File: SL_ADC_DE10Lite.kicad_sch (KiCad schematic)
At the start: 21 parts, among them J1 Conn_02x20_Odd_Even, J2 Conn_02x08_Odd_Even, J3 Conn_02x05_Counter_Clockwise, J5 Conn_02x07_Counter_Clockwise

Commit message: Update net names
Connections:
- net CH_C1: now also IC1.63 (REFCP)
- net DGND: no longer IC1.36 (ASLEEP)
- net REFCP: no longer IC1.63 (REFCP)
- net ASLEEP: now reaches J1.21 (Pin_21)
- net ASLEEP: now also IC1.36 (ASLEEP)
- net GPIO(23)-REFIN/~{WR} renamed GPIO(23)-REFEN/~{WR}
- no-connect marks 7 -> 6
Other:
- moved on the sheet: J2, J3, J5
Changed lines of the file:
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@@
 		(at 44.45 176.53)
 	)
-	(no_connect
-		(at 44.45 156.21)
-	)
 	(wire
 		(pts
@@
 	)
 	(label "CH_A0"
-		(at 102.87 130.81 0)
+		(at 104.14 132.08 0)
 		(effects
 			(font
@@
 	)
 	(label "DGND"
-		(at 102.87 162.56 0)
+		(at 104.14 163.83 0)
 		(effects
 			(font
@@
 	)
 	(label "CH_D0"
-		(at 90.17 146.05 180)
+		(at 91.44 147.32 180)
 		(effects
 			(font
@@
 	)
 	(label "CH_D0"
-		(at 102.87 146.05 0)
+		(at 104.14 147.32 0)
 		(effects
 			(font
@@
 	)
 	(label "DGND"
-		(at 102.87 165.1 0)
+		(at 104.14 166.37 0)
 		(effects
 			(font
@@
 		)
 	)
-	(label "GPIO(23)-REFIN{slash}~{WR}"
+	(label "GPIO(23)-REFEN{slash}~{WR}"
 		(at 57.15 161.29 0)
 		(effects
@@
 		)
 	)
-	(label "GPIO(23)-REFIN{slash}~{WR}"
+	(label "GPIO(23)-REFEN{slash}~{WR}"
 		(at 43.18 67.31 180)
 		(effects
@@
 	)
 	(label "CH_C1"
-		(at 102.87 143.51 0)
+		(at 104.14 144.78 0)
 		(effects
 			(font
@@
 	)
 	(label "CH_A1"
-		(at 90.17 133.35 180)
+		(at 91.44 134.62 180)
 		(effects
 			(font
@@
 	)
 	(label "HVSS"
-		(at 134.62 163.83 0)
+		(at 135.89 165.1 0)
 		(effects
 			(font
@@
 	)
 	(label "AGND"
-		(at 121.92 173.99 180)
+		(at 123.19 175.26 180)
 		(effects
 			(font
@@
 	)
 	(label "AGND"
-		(at 134.62 166.37 0)
+		(at 135.89 167.64 0)
 		(effects
 			(font
@@
 	)
 	(label "HVDD"
-		(at 121.92 158.75 180)
+		(at 123.19 160.02 180)
 		(effects
 			(font
@@
 		)
 	)
+	(label "ASLEEP"
+		(at 44.45 156.21 180)
+		(effects
+			(font
+				(size 1.27 1.27)
+			)
+			(justify right bottom)
+		)
+	)
 	(label "CH_B0"
-		(at 102.87 135.89 0)
+		(at 104.14 137.16 0)
 		(effects
 			(font
@@
 	)
 	(label "DGND"
-		(at 90.17 170.18 180)
+		(at 91.44 171.45 180)
 		(effects
 			(font
@@
 	)
 	(label "DGND"
-		(at 90.17 167.64 180)
+		(at 91.44 168.91 180)
 		(effects
 			(font
@@
 	)
 	(label "CH_C0"
-		(at 90.17 140.97 180)
+		(at 91.44 142.24 180)
 		(effects
 			(font
@@
 	)
 	(label "DGND"
-		(at 102.87 172.72 0)
+		(at 104.14 173.99 0)
 		(effects
 			(font
@@
 	)
 	(label "CH_B1"
-		(at 102.87 138.43 0)
+		(at 104.14 139.7 0)
 		(effects
 			(font
@@
 	)
 	(label "CH_C1"
-		(at 90.17 143.51 180)
+		(at 91.44 144.78 180)
 		(effects
 			(font
@@
 	)
 	(label "DGND"
-		(at 90.17 172.72 180)
+		(at 91.44 173.99 180)
 		(effects
 			(font
@@
 	)
 	(label "DGND"
-		(at 90.17 162.56 180)
+		(at 91.44 163.83 180)
 		(effects
 			(font
@@
 	)
 	(label "DGND"
-		(at 102.87 167.64 0)
+		(at 104.14 168.91 0)
 		(effects
 			(font
@@
 	)
 	(label "AVDD"
-		(at 121.92 161.29 180)
+		(at 123.19 162.56 180)
 		(effects
 			(font
@@
 	)
 	(label "AGND"
-		(at 134.62 171.45 0)
+		(at 135.89 172.72 0)
 		(effects
 			(font
@@
 	)
 	(label "HVDD"
-		(at 134.62 158.75 0)
+		(at 135.89 160.02 0)
 		(effects
 			(font
@@
 	)
 	(label "HVSS"
-		(at 121.92 163.83 180)
+		(at 123.19 165.1 180)
 		(effects
 			(font
@@
 	)
 	(label "CH_A0"
-		(at 90.17 130.81 180)
+		(at 91.44 132.08 180)
 		(effects
 			(font
@@
 	)
 	(label "CH_B0"
-		(at 90.17 135.89 180)
+		(at 91.44 137.16 180)
 		(effects
 			(font
@@
 	)
 	(label "DGND"
-		(at 90.17 165.1 180)
+		(at 91.44 166.37 180)
 		(effects
 			(font
@@
 	)
 	(label "CH_D1"
-		(at 102.87 148.59 0)
+		(at 104.14 149.86 0)
 		(effects
 			(font
@@
 	)
 	(label "AGND"
-		(at 121.92 168.91 180)
+		(at 123.19 170.18 180)
 		(effects
 			(font
@@
 		)
 	)
-	(label "DGND"
+	(label "ASLEEP"
 		(at 116.84 72.39 0)
 		(effects
@@
 	)
 	(label "CH_C0"
-		(at 102.87 140.97 0)
+		(at 104.14 142.24 0)
 		(effects
 			(font
@@
 	)
 	(label "CH_B1"
-		(at 90.17 138.43 180)
+		(at 91.44 139.7 180)
 		(effects
 			(font
@@
 	)
 	(label "CH_A1"
-		(at 102.87 133.35 0)
+		(at 104.14 134.62 0)
 		(effects
 			(font
@@
 	)
 	(label "AGND"
-		(at 134.62 173.99 0)
+		(at 135.89 175.26 0)
 		(effects
 			(font
@@
 	)
 	(label "AGND"
-		(at 121.92 171.45 180)
+		(at 123.19 172.72 180)
 		(effects
 			(font
@@
 	)
 	(label "AGND"
-		(at 121.92 166.37 180)
+		(at 123.19 167.64 180)
 		(effects
 			(font
@@
 		)
 	)
-	(label "REFCP"
+	(label "CH_C1"
 		(at 63.5 36.83 90)
 		(effects
@@
 	)
 	(label "AVDD"
-		(at 134.62 161.29 0)
+		(at 135.89 162.56 0)
 		(effects
 			(font
@@
 	)
 	(label "CH_D1"
-		(at 90.17 148.59 180)
+		(at 91.44 149.86 180)
 		(effects
 			(font
@@
 	)
 	(label "AGND"
-		(at 134.62 168.91 0)
+		(at 135.89 170.18 0)
 		(effects
 			(font
@@
 	)
 	(label "DGND"
-		(at 102.87 170.18 0)
+		(at 104.14 171.45 0)
 		(effects
 			(font
@@
 	(symbol
 		(lib_id "Connector_Generic:Conn_02x05_Counter_Clockwise")
-		(at 95.25 167.64 0)
+		(at 96.52 168.91 0)
 		(unit 1)
 		(body_style 1)
@@
 		(fields_autoplaced yes)
 		(property "Reference" "J3"
-			(at 96.52 156.21 0)
+			(at 97.79 157.48 0)
 			(show_name no)
 			(do_not_autoplace no)
@@
 		)
 		(property "Value" "Conn_02x05_Counter_Clockwise"
-			(at 96.52 158.75 0)
+			(at 97.79 160.02 0)
 			(show_name no)
 			(do_not_autoplace no)
@@
 		)
 		(property "Footprint" "Connector_PinHeader_2.54mm:PinHeader_2x05_P2.54mm_Vertical"
-			(at 95.25 167.64 0)
+			(at 96.52 168.91 0)
 			(hide yes)
 			(show_name no)
@@
 		)
 		(property "Datasheet" ""
-			(at 95.25 167.64 0)
+			(at 96.52 168.91 0)
 			(hide yes)
 			(show_name no)
@@
 		)
 		(property "Description" "Generic connector, double row, 02x05, counter clockwise pin numbering scheme (similar to DIP package numbering), script generated (kicad-library-utils/schlib/autogen/connector/)"
-			(at 95.25 167.64 0)
+			(at 96.52 168.91 0)
 			(hide yes)
 			(show_name no)
@@
 	(symbol
 		(lib_id "Connector_Generic:Conn_02x07_Counter_Clockwise")
-		(at 127 166.37 0)
+		(at 128.27 167.64 0)
 		(unit 1)
 		(body_style 1)
@@
 		(fields_autoplaced yes)
 		(property "Reference" "J5"
-			(at 128.27 152.4 0)
+			(at 129.54 153.67 0)
 			(show_name no)
 			(do_not_autoplace no)
@@
 		)
 		(property "Value" "Conn_02x07_Counter_Clockwise"
-			(at 128.27 154.94 0)
+			(at 129.54 156.21 0)
 			(show_name no)
 			(do_not_autoplace no)
@@
 		)
 		(property "Footprint" ""
-			(at 127 166.37 0)
+			(at 128.27 167.64 0)
 			(hide yes)
 			(show_name no)
@@
 		)
 		(property "Datasheet" ""
-			(at 127 166.37 0)
+			(at 128.27 167.64 0)
 			(hide yes)
 			(show_name no)
@@
 		)
 		(property "Description" "Generic connector, double row, 02x07, counter clockwise pin numbering scheme (similar to DIP package numbering), script generated (kicad-library-utils/schlib/autogen/connector/)"
-			(at 127 166.37 0)
+			(at 128.27 167.64 0)
 			(hide yes)
 			(show_name no)
@@
 	(symbol
 		(lib_id "Connector_Generic:Conn_02x08_Odd_Even")
-		(at 95.25 138.43 0)
+		(at 96.52 139.7 0)
 		(unit 1)
 		(body_style 1)
@@
 		(fields_autoplaced yes)
 		(property "Reference" "J2"
-			(at 96.52 124.46 0)
+			(at 97.79 125.73 0)
 			(show_name no)
 			(do_not_autoplace no)
@@
 		)
 		(property "Value" "Conn_02x08_Odd_Even"
-			(at 96.52 127 0)
+			(at 97.79 128.27 0)
 			(show_name no)
 			(do_not_autoplace no)
@@
 		)
 		(property "Footprint" "Connector_PinHeader_2.54mm:PinHeader_2x08_P2.54mm_Vertical"
-			(at 95.25 138.43 0)
+			(at 96.52 139.7 0)
 			(hide yes)
 			(show_name no)
@@
 		)
 		(property "Datasheet" ""
-			(at 95.25 138.43 0)
+			(at 96.52 139.7 0)
 			(hide yes)
 			(show_name no)
@@
 		)
 		(property "Description" "Generic connector, double row, 02x08, odd/even pin numbering scheme (row 1 odd numbers, row 2 even numbers), script generated (kicad-library-utils/schlib/autogen/connector/)"
-			(at 95.25 138.43 0)
+			(at 96.52 139.7 0)
 			(hide yes)
 			(show_name no)

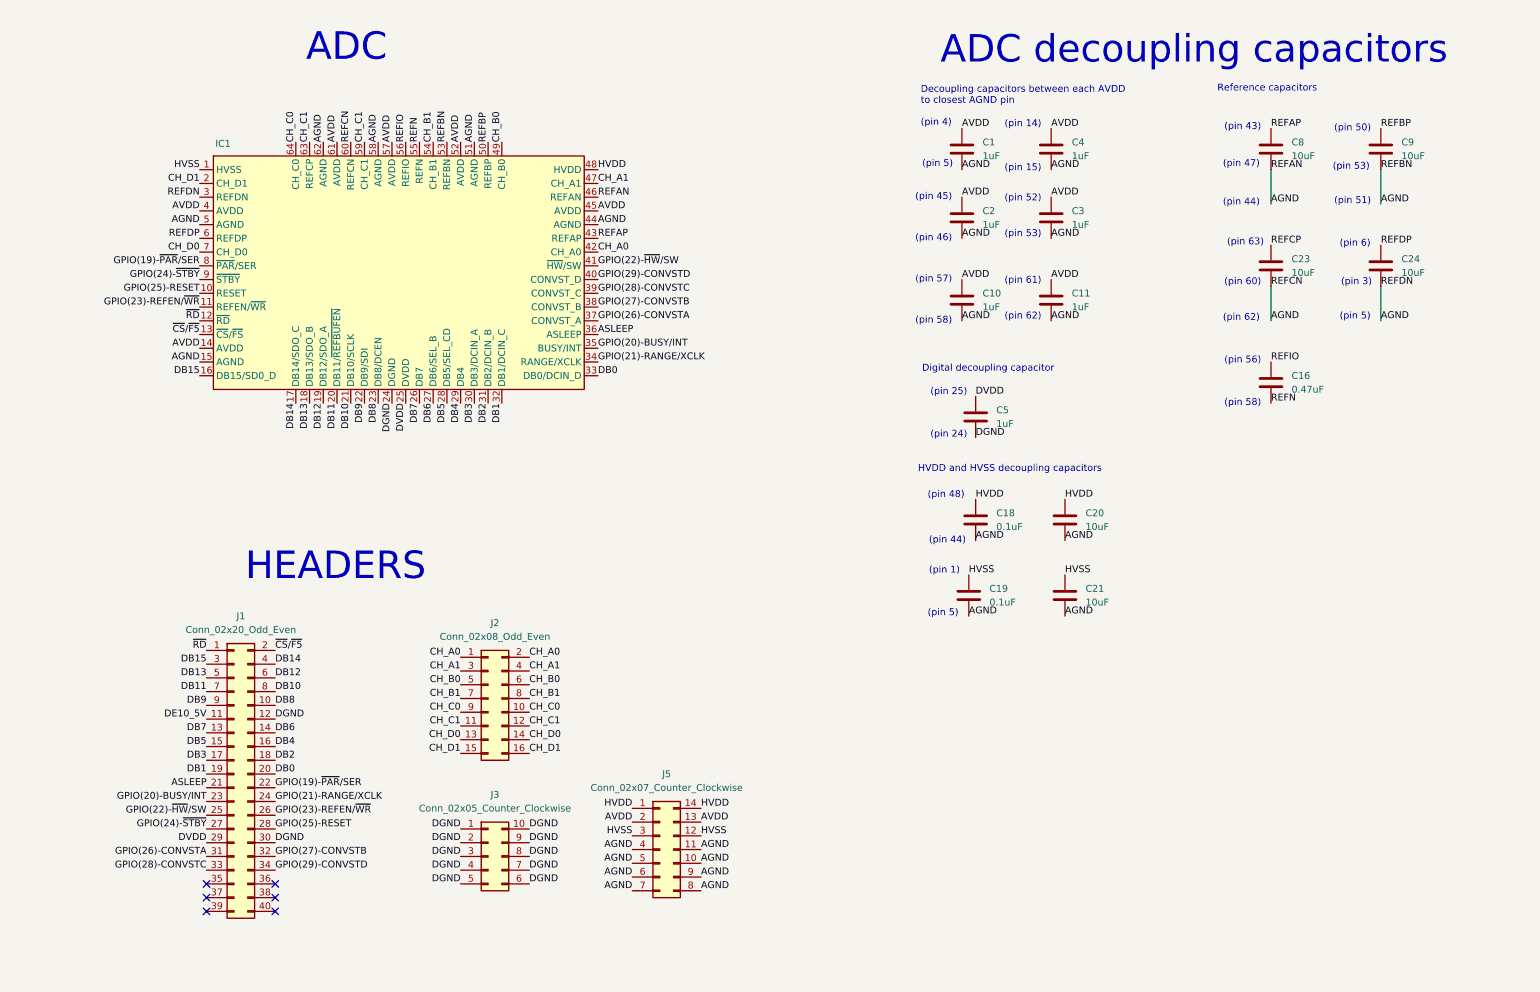
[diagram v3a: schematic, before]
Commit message: Add analog header
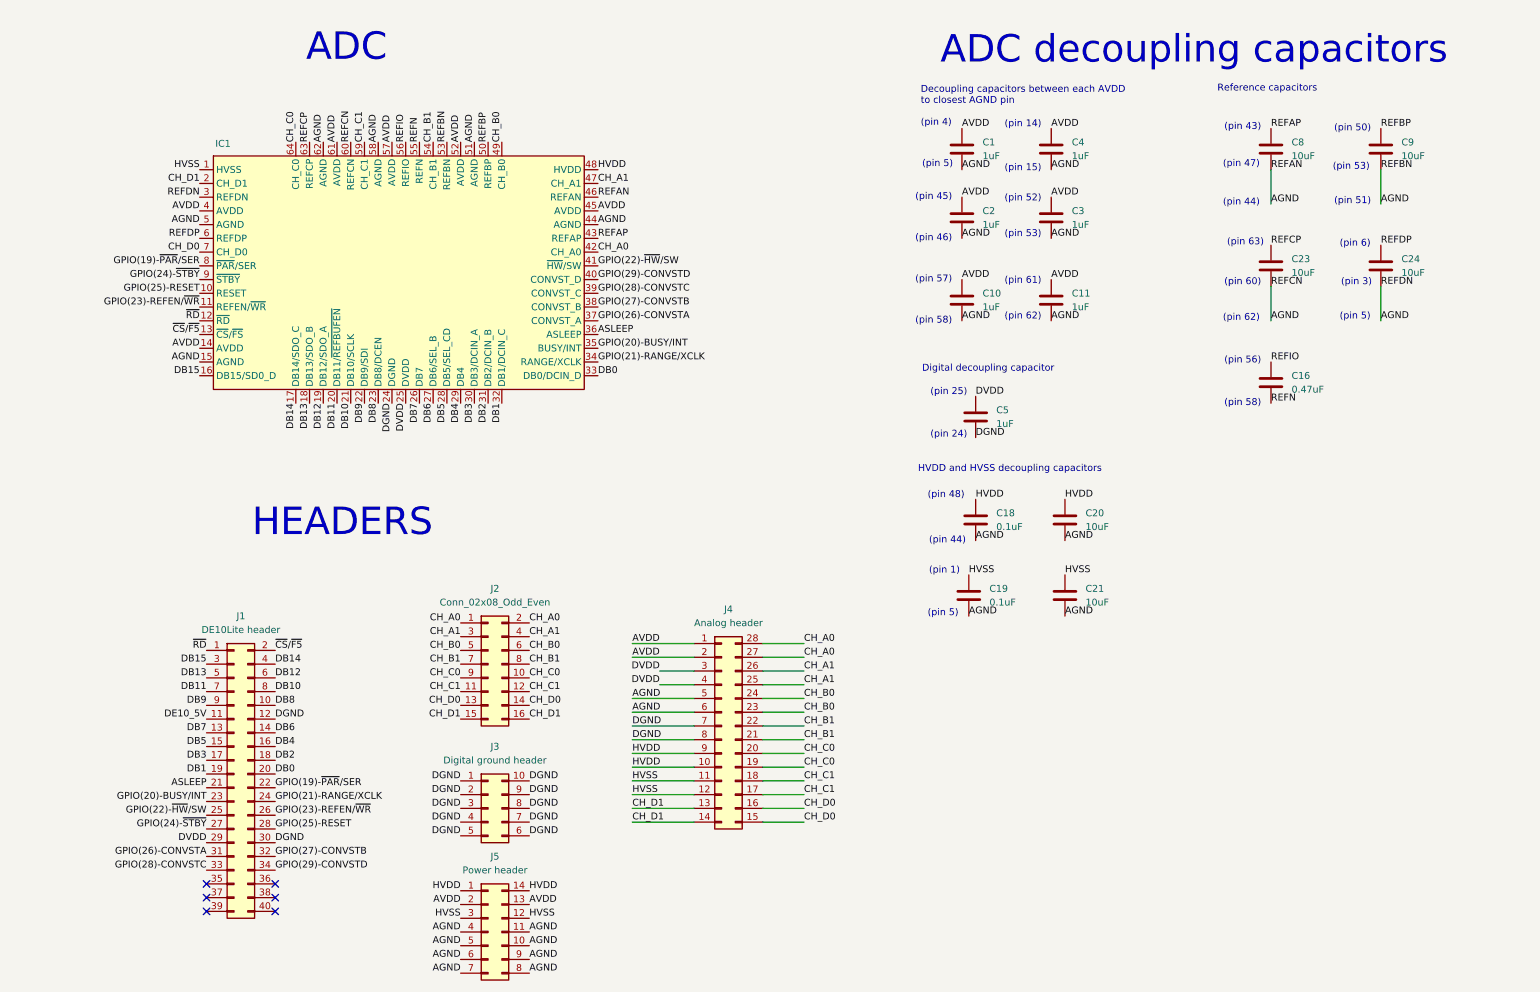
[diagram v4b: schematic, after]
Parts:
- added J4: Analog header, Connector_PinHeader_2.54mm:PinHeader_2x14_P2.54mm_Vertical, symbol Connector_Generic:Conn_02x14_Counter_Clockwise
- J1: value Conn_02x20_Odd_Even -> DE10Lite header
- J3: value Conn_02x05_Counter_Clockwise -> Digital ground header
- J5: value Conn_02x07_Counter_Clockwise -> Power header
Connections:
- net AGND: now also J4.5 (Pin_5), J4.6 (Pin_6)
- net AVDD: now also J4.1 (Pin_1), J4.2 (Pin_2)
- net CH_A0: now also J4.27 (Pin_27), J4.28 (Pin_28)
- net CH_A1: now also J4.25 (Pin_25), J4.26 (Pin_26)
- net CH_B0: now also J4.23 (Pin_23), J4.24 (Pin_24)
- net CH_B1: now also J4.21 (Pin_21), J4.22 (Pin_22)
- net CH_C0: now also J4.19 (Pin_19), J4.20 (Pin_20)
- net CH_C1: now also J4.17 (Pin_17), J4.18 (Pin_18); no longer IC1.63 (REFCP)
- net CH_D0: now also J4.15 (Pin_15), J4.16 (Pin_16)
- net CH_D1: now also J4.13 (Pin_13), J4.14 (Pin_14)
- net DGND: now also J4.7 (Pin_7), J4.8 (Pin_8)
- net DVDD: now also J4.3 (Pin_3), J4.4 (Pin_4)
- net HVDD: now also J4.10 (Pin_10), J4.9 (Pin_9)
- net HVSS: now also J4.11 (Pin_11), J4.12 (Pin_12)
- net REFCP: now also IC1.63 (REFCP)
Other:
- moved on the sheet: J2, J3, J5
